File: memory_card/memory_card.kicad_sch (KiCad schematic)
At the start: 22 parts, among them IC1 SN74HCT138N, IC2 SN74HCT138N, J1 Conn1, U1 AS6C4008-55PCN, U2 74HCT374, U3 74HCT32, U4 74HCT00, U5 ZIF_AT28CXXX, U6 74HCT04, U7 74HCT374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

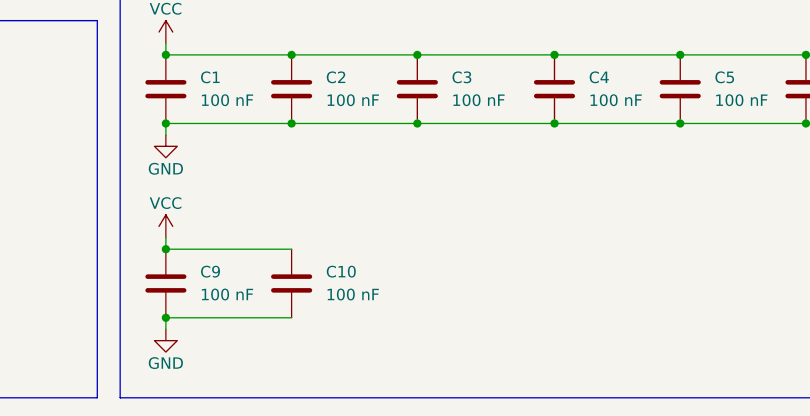
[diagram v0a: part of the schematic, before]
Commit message: Added missing decoupling capacitor to U6. Also reorganzied all decoupling capacitor's reference value to make it flow better on the PCB
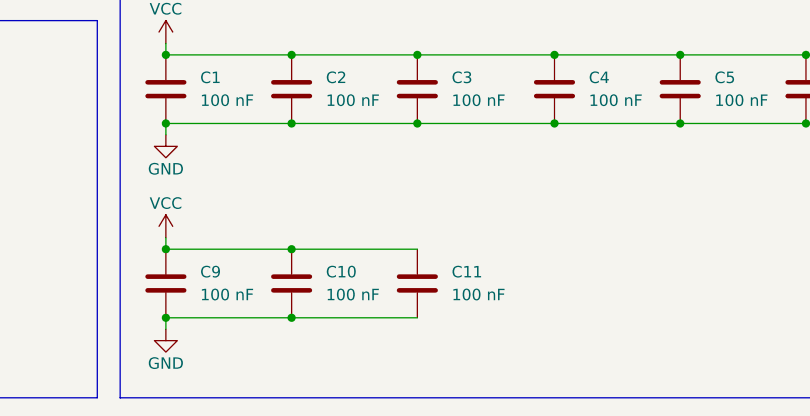
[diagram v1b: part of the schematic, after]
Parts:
- added C11: 100 nF, Capacitor_THT:C_Disc_D3.0mm_W1.6mm_P2.50mm, symbol Device:C
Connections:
- net GND: now also C11.2
- net VCC: now also C11.1
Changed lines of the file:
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@@
 	)
 	(junction
+		(at 138.43 248.92)
+		(diameter 0)
+		(color 0 0 0 0)
+	)
+	(junction
 		(at 124.46 248.92)
 		(diameter 0)
@@
 	)
 	(junction
+		(at 138.43 256.54)
+		(diameter 0)
+		(color 0 0 0 0)
+	)
+	(junction
 		(at 52.07 243.84)
 		(diameter 0)
@@
 		)
 	)
+	(wire
+		(pts
+			(xy 138.43 256.54) (xy 152.4 256.54)
+		)
+		(stroke
+			(width 0)
+			(type default)
+		)
+	)
 	(bus
 		(pts
@@
 		)
 	)
+	(wire
+		(pts
+			(xy 138.43 248.92) (xy 152.4 248.92)
+		)
+		(stroke
+			(width 0)
+			(type default)
+		)
+	)
 	(bus
 		(pts
@@
 					(unit 1)
 				)
+			)
+		)
+	)
+	(symbol
+		(lib_id "Device:C")
+		(at 152.4 252.73 0)
+		(unit 1)
+		(exclude_from_sim no)
+		(in_bom yes)
+		(on_board yes)
+		(dnp no)
+		(fields_autoplaced yes)
+		(property "Reference" "C11"
+			(at 156.21 251.4599 0)
+			(effects
+				(font
+					(size 1.27 1.27)
+				)
+				(justify left)
+			)
+		)
+		(property "Value" "100 nF"
+			(at 156.21 253.9999 0)
+			(effects
+				(font
+					(size 1.27 1.27)
+				)
+				(justify left)
+			)
+		)
+		(property "Footprint" "Capacitor_THT:C_Disc_D3.0mm_W1.6mm_P2.50mm"
+			(at 153.3652 256.54 0)
+			(effects
+				(font
+					(size 1.27 1.27)
+				)
+				(hide yes)
+			)
+		)
+		(property "Datasheet" "~"
+			(at 152.4 252.73 0)
+			(effects
+				(font
+					(size 1.27 1.27)
+				)
+				(hide yes)
+			)
+		)
+		(property "Description" ""
+			(at 152.4 252.73 0)
+			(effects
+				(font
+					(size 1.27 1.27)
+				)
+				(hide yes)
+			)
+		)
+		(pin "1"
+		)
+		(pin "2"
+		)
+		(instances
+			(project "memory_card"
+				(path "/7e612cd7-4917-4f54-9218-de1e55bc57f9"
+					(reference "C11")
+					(unit 1)
+				)
